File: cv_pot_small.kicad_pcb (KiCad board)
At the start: 2 copper layers, 24 x 17 mm, 14 parts, among them J1 I/O connector, U1 HT7550-1, U2 TLV6001UIDBVR

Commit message: Reduce solder mask expansion to 0.05mm to fix aperture-bridge DRC
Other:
- rule pad_to_mask_clearance: 0.2 -> 0.05
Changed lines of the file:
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@@
       (dielectric_constraints no)
     )
-    (pad_to_mask_clearance 0.2)
+    (pad_to_mask_clearance 0.05)
     (pcbplotparams
       (layerselection 0x00010f0_ffffffff)

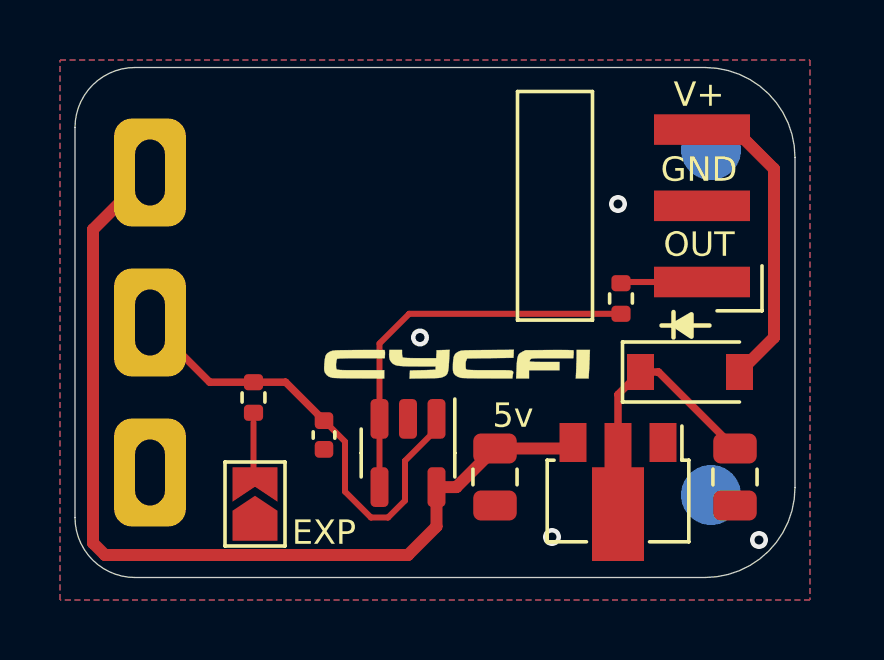
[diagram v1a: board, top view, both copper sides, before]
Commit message: Convert the small CV pot to the 3.3V CV port standard
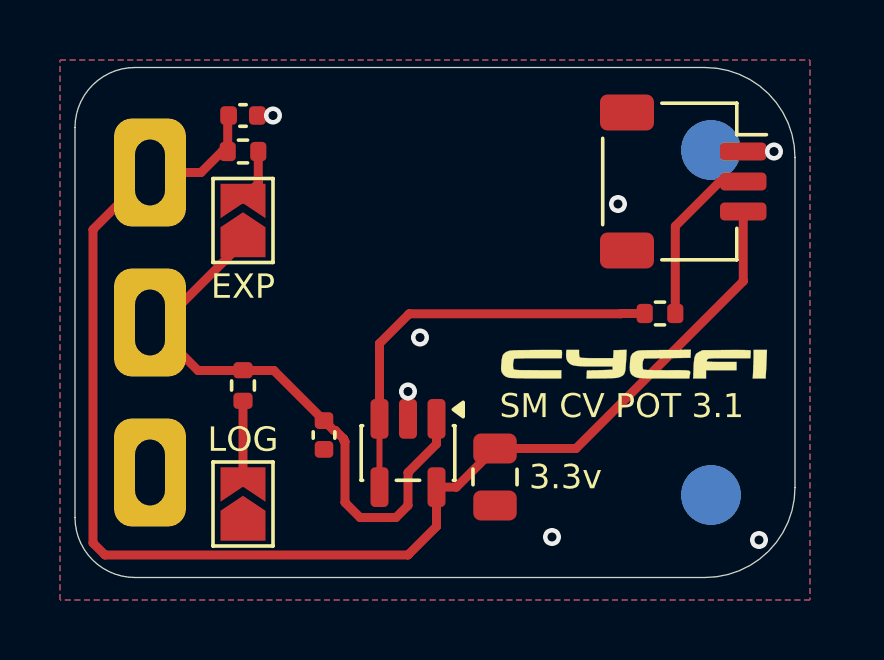
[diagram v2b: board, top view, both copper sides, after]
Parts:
- removed C1: 10uF, Capacitor_SMD:C_0805_2012Metric
- removed D1: 1N4148W, Diode_SMD:D_SOD-123
- removed U1: HT7550-1, Package_TO_SOT_SMD:SOT-89-3
- added C4: 100nF, Capacitor_SMD:C_0402_1005Metric, F.Cu at (142.6, 73.6)
- added JP2: exp shunt, Jumper:SolderJumper-2_P1.3mm_Open_TrianglePad1.0x1.5mm, F.Cu at (142.6, 77.1)
- added R3: 47k, Resistor_SMD:R_0402_1005Metric, F.Cu at (142.6, 74.8)
- J1: footprint cycfi_library:pin_header_1x3p_2.54mm_smd_horizontal -> Connector_JST:JST_SH_SM03B-SRSS-TB_1x03-1MP_P1.00mm_Horizontal
- JP1: value exp shunt -> log shunt
- R2: value 1k -> 200Ω
- moved G*** 5.90 mm to (155.6, 81.9)
- moved J1 3.41 mm to (157.3, 75.8), turned to -90 degrees
- moved R2 1.39 mm to (156.5, 80.2), turned to 0 degrees
- moved R1 0.53 mm to (142.6, 82.6)
- moved JP1 0.40 mm to (142.6, 86.5)
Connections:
- C2 pad 1: 5v -> +3V3
- J1 pad 1: OUT -> GND
- J1 pad 2: GND -> /OUT
- J1 pad 3: V+ -> +3V3
- R2 pad 2: OUT -> /OUT
- RV1 pad 1: 5v -> +3V3
- U2 pad 5: 5v -> +3V3
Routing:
- net +3V3: track 0.00 -> 45.9 mm
- net 5v: track 31.6 -> 0.00 mm
- net V+: track 10.2 -> 0.00 mm
- net Net-(C1-Pad1): track 6.95 -> 0.00 mm
- net /OUT: track 0.00 -> 5.79 mm
- net /pot_center: track 15.6 -> 20.2 mm
- net OUT: track 2.72 -> 0.00 mm
- net GND: track 0.00 -> 2.46 mm, vias 4 -> 7
- net Net-(JP2-B): track 0.00 -> 1.79 mm
- net Net-(U2--): track 13.2 -> 14.0 mm
- net Net-(JP1-B): track 2.02 -> 2.72 mm
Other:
- board text added: "3.3v"
- board text added: "LOG"
- board text added: "SM CV POT 3.1"
- board text removed: "5v"
- board text removed: "GND"
- board text removed: "OUT"
- board text removed: "V+"
